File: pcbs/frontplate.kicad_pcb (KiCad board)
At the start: 2 copper layers, 129.8 x 107.9 mm, 5 parts

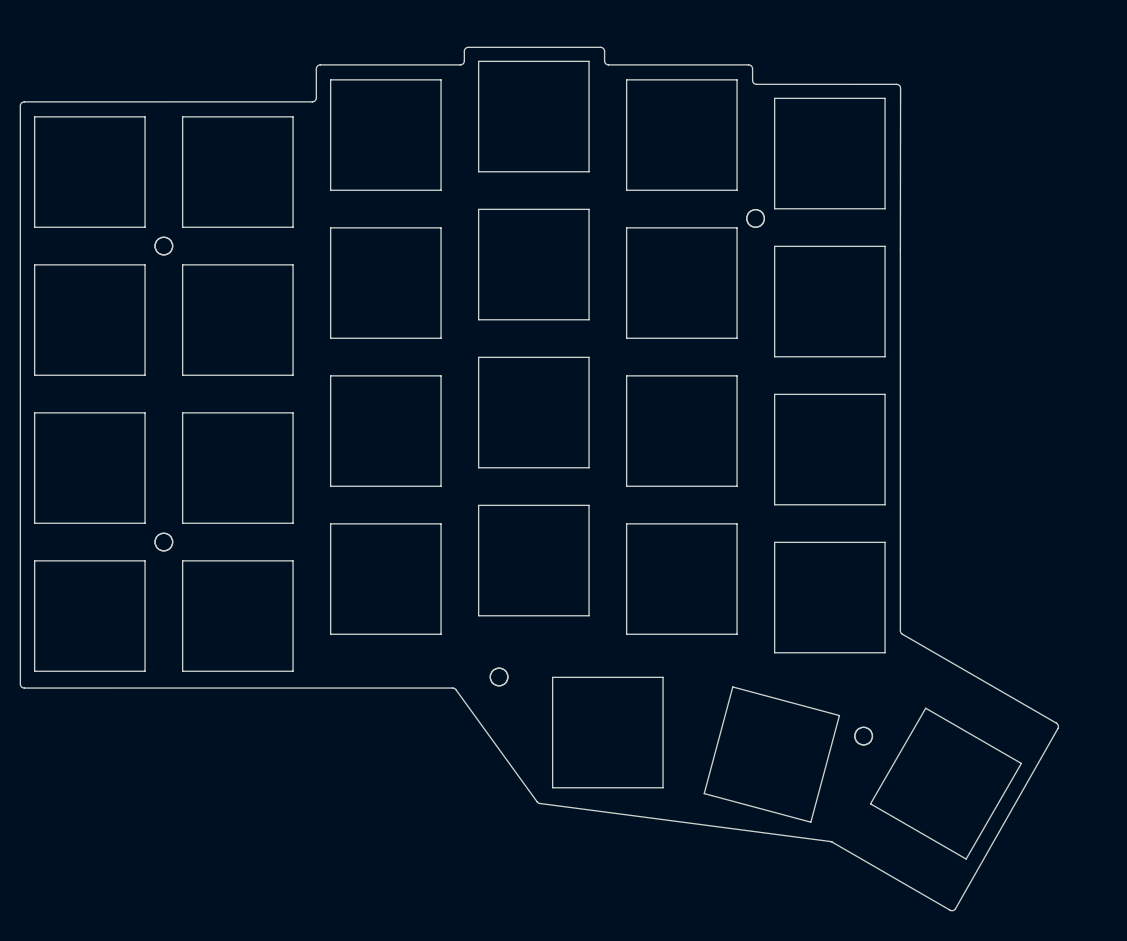
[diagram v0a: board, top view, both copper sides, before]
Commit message: fix(pcb): increase key spacing and correct power switch
Set the PG1316S key pitch to 19.5 mm in both axes and regenerate the tracked PCB and outline artifacts.

Keep the power switch mapping consistent with the intended on/off orientation while preserving the original board outline.
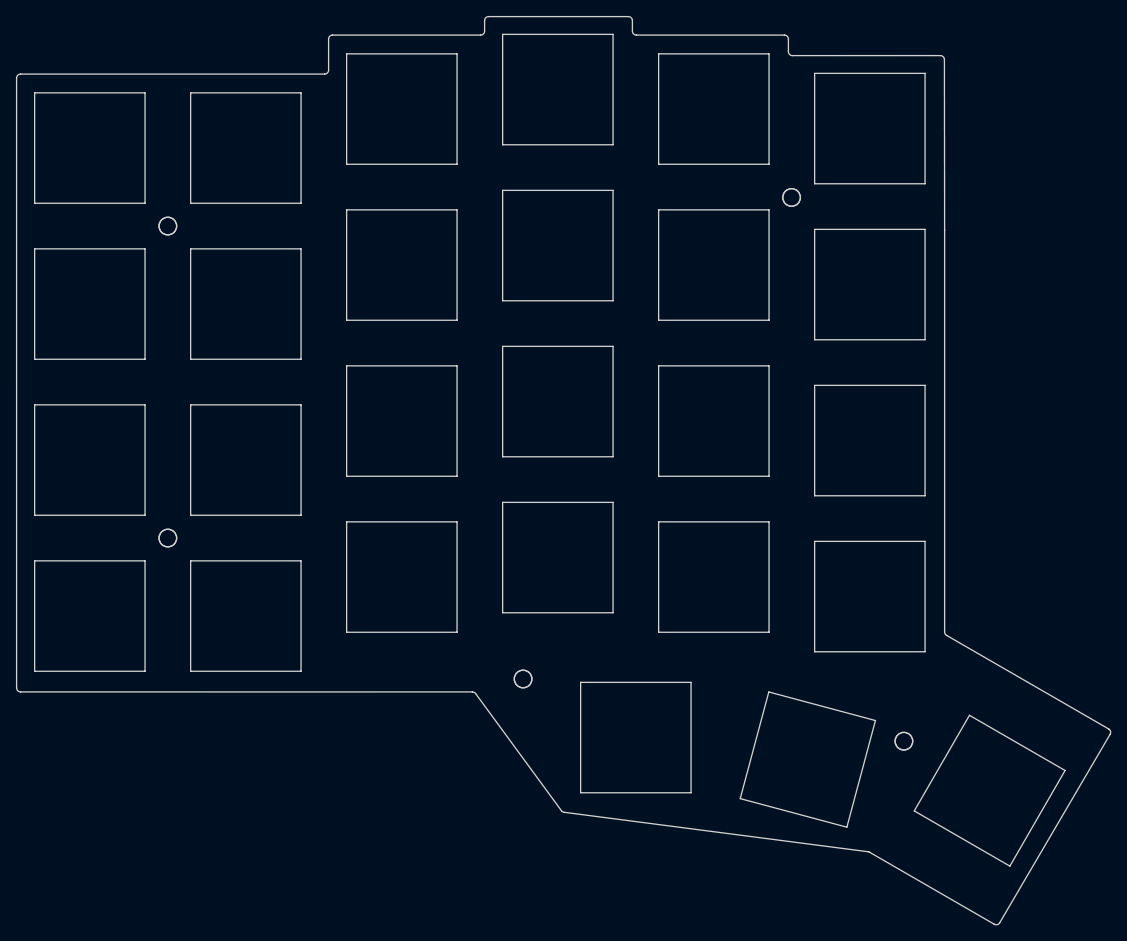
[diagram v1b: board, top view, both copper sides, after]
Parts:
- moved MH3 5.21 mm to (187.7, 47.7)
- moved MH5 5.07 mm to (201.8, 115.6)
- moved MH4 3.01 mm to (154.2, 107.9)
- moved MH1 2.55 mm to (109.8, 51.2)
- moved MH2 0.71 mm to (109.8, 90.2)
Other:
- board size 129.8 x 107.9 mm -> 136.8 x 113.5 mm

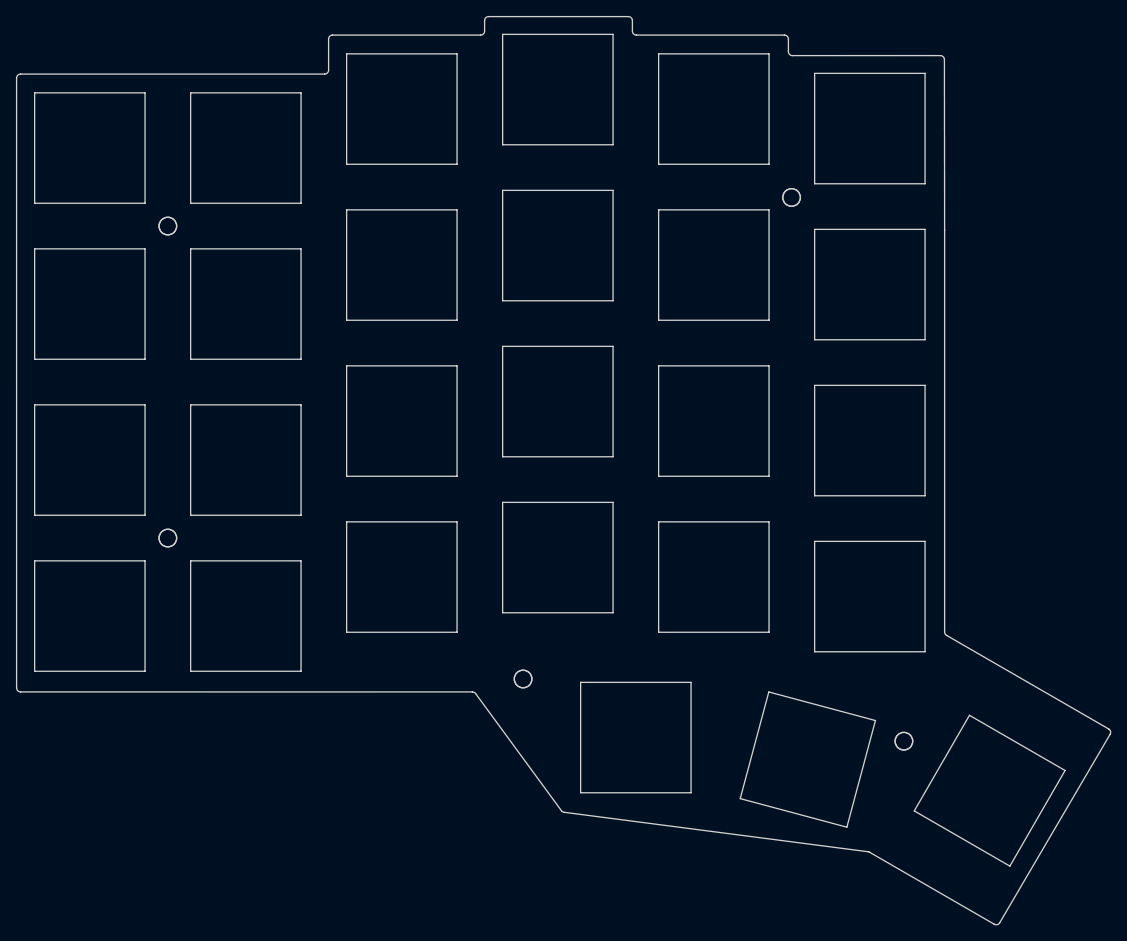
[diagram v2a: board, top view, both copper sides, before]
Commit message: feat: default to compact 18.5 mm layout and refresh generated boards
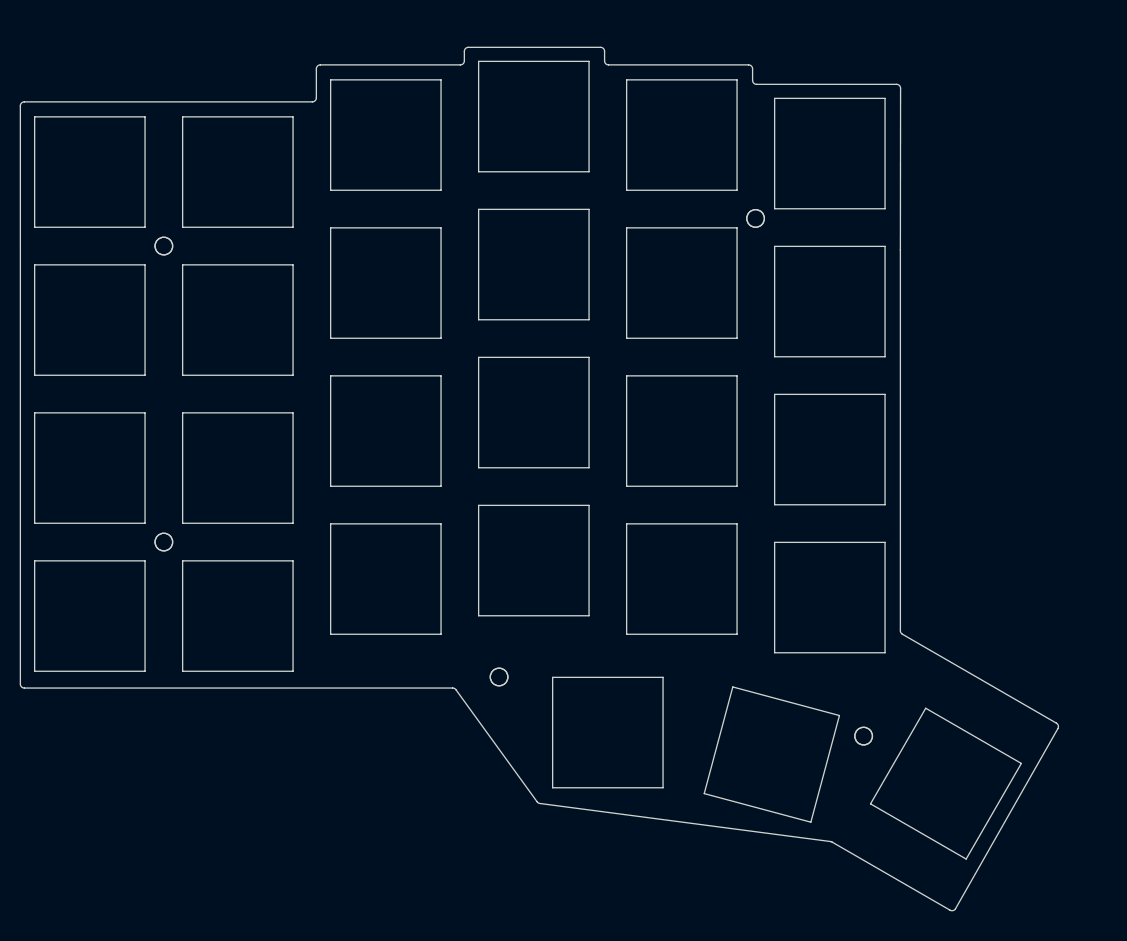
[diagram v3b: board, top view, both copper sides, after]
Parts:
- moved MH3 5.21 mm to (183.2, 50.3)
- moved MH5 5.07 mm to (196.7, 115.0)
- moved MH4 3.01 mm to (151.2, 107.6)
- moved MH1 2.55 mm to (109.2, 53.8)
- moved MH2 0.71 mm to (109.2, 90.8)
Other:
- board size 136.8 x 113.5 mm -> 129.8 x 107.9 mm
